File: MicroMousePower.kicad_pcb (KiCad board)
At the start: 2 copper layers, 59.6 x 56 mm, 103 parts, among them J1 USB_C_Receptacle_PowerOnly_6P, J2 Conn_02x16_Odd_Even, J3 Conn_01x02_Pin, Q1 TIP41C, Q2 TIP41C, Q3 TIP41C, U1 INA219AxDCN, U2 MCP73831-3-MC, U3 CH224K, U4 DRV8833PWPR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

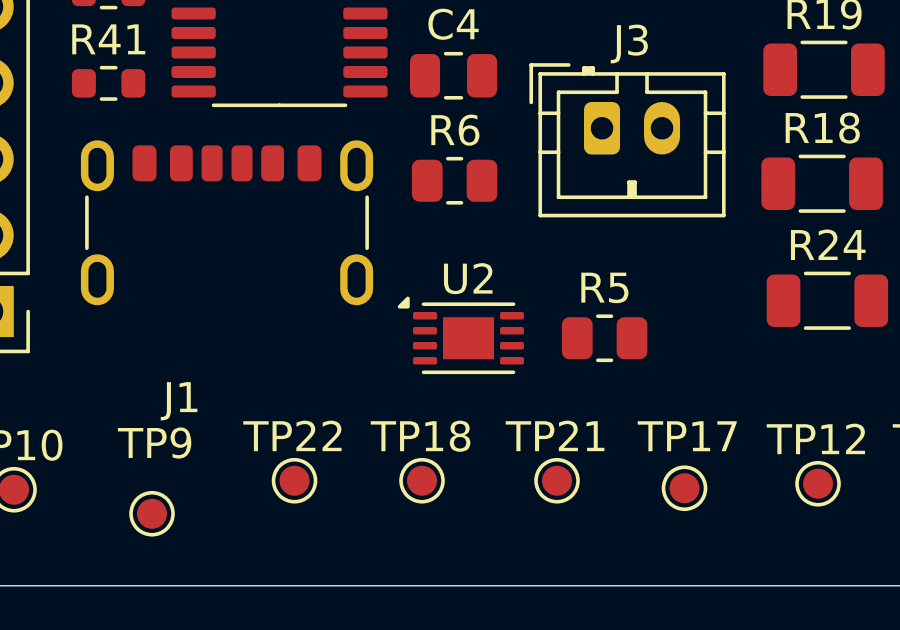
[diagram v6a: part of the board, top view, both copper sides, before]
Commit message: fixed another disconnect
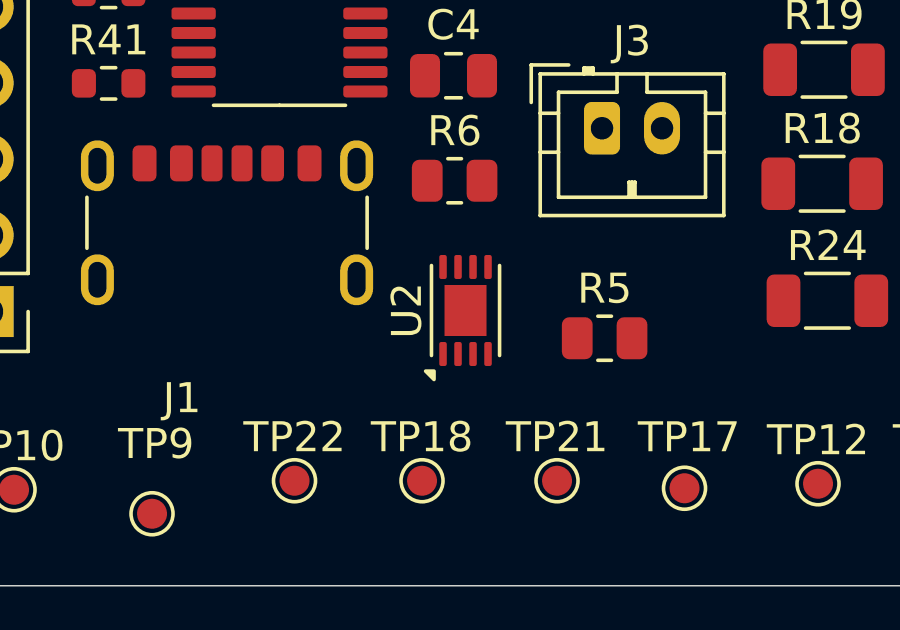
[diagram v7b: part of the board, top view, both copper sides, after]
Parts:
- moved U2 0.93 mm to (168.4, 108.8), turned to 90 degrees
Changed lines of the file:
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@@
 	(footprint "Package_DFN_QFN:DFN-8-1EP_3x2mm_P0.5mm_EP1.7x1.4mm"
 		(layer "F.Cu")
-		(at 168.55 109.75)
+		(at 168.45 108.825 90)
 		(descr "DFN, 8 Pin (http://ww1.microchip.com/downloads/en/DeviceDoc/8L_DFN_2x3x0_9_MC_C04-123C.pdf), generated with kicad-footprint-generator ipc_noLead_generator.py")
 		(tags "DFN NoLead")
 		(property "Reference" "U2"
-			(at 0 -1.95 0)
+			(at 0 -1.95 90)
 			(layer "F.SilkS")
 			(effects
@@
 		)
 		(property "Value" "MCP73831-3-MC"
-			(at 0 1.95 0)
+			(at 0 1.95 90)
 			(layer "F.Fab")
 			(effects
@@
 		)
 		(property "Datasheet" "http://ww1.microchip.com/downloads/en/DeviceDoc/20001984g.pdf"
-			(at 0 0 0)
+			(at 0 0 90)
 			(layer "F.Fab")
 			(hide yes)
@@
 		)
 		(property "Description" "Single cell, Li-Ion/Li-Po charge management controller, 4.35V, Tri-State Status Output, in DFN-8 package"
-			(at 0 0 0)
+			(at 0 0 90)
 			(layer "F.Fab")
 			(hide yes)
@@
 		)
 		(property "LCSC" "C635038"
-			(at 0 0 0)
+			(at 0 0 90)
 			(unlocked yes)
 			(layer "F.Fab")
@@
 		)
 		(fp_line
+			(start 2.1 -1.25)
+			(end -2.1 -1.25)
+			(stroke
+				(width 0.05)
+				(type solid)
+			)
+			(layer "F.CrtYd")
+		)
+		(fp_line
 			(start -2.1 -1.25)
 			(end -2.1 1.25)
@@
 		)
 		(fp_line
+			(start 2.1 1.25)
+			(end 2.1 -1.25)
+			(stroke
+				(width 0.05)
+				(type solid)
+			)
+			(layer "F.CrtYd")
+		)
+		(fp_line
 			(start -2.1 1.25)
 			(end 2.1 1.25)
@@
 		)
 		(fp_line
-			(start 2.1 -1.25)
-			(end -2.1 -1.25)
-			(stroke
-				(width 0.05)
-				(type solid)
-			)
-			(layer "F.CrtYd")
-		)
-		(fp_line
-			(start 2.1 1.25)
-			(end 2.1 -1.25)
-			(stroke
-				(width 0.05)
-				(type solid)
-			)
-			(layer "F.CrtYd")
+			(start 1.5 -1)
+			(end 1.5 1)
+			(stroke
+				(width 0.1)
+				(type solid)
+			)
+			(layer "F.Fab")
+		)
+		(fp_line
+			(start -1 -1)
+			(end 1.5 -1)
+			(stroke
+				(width 0.1)
+				(type solid)
+			)
+			(layer "F.Fab")
 		)
 		(fp_line
@@
 		)
 		(fp_line
+			(start 1.5 1)
+			(end -1.5 1)
+			(stroke
+				(width 0.1)
+				(type solid)
+			)
+			(layer "F.Fab")
+		)
+		(fp_line
 			(start -1.5 1)
 			(end -1.5 -0.5)
@@
 			(layer "F.Fab")
 		)
-		(fp_line
-			(start -1 -1)
-			(end 1.5 -1)
-			(stroke
-				(width 0.1)
-				(type solid)
-			)
-			(layer "F.Fab")
-		)
-		(fp_line
-			(start 1.5 -1)
-			(end 1.5 1)
-			(stroke
-				(width 0.1)
-				(type solid)
-			)
-			(layer "F.Fab")
-		)
-		(fp_line
-			(start 1.5 1)
-			(end -1.5 1)
-			(stroke
-				(width 0.1)
-				(type solid)
-			)
-			(layer "F.Fab")
-		)
 		(fp_text user "${REFERENCE}"
-			(at 0 0 0)
+			(at 0 0 90)
 			(layer "F.Fab")
 			(effects
@@
 		)
 		(pad "" smd roundrect
-			(at -0.425 -0.35)
-			(size 0.69 0.56)
-			(layers "F.Paste")
-			(roundrect_rratio 0.25)
-		)
-		(pad "" smd roundrect
-			(at -0.425 0.35)
-			(size 0.69 0.56)
-			(layers "F.Paste")
-			(roundrect_rratio 0.25)
-		)
-		(pad "" smd roundrect
-			(at 0.425 -0.35)
-			(size 0.69 0.56)
-			(layers "F.Paste")
-			(roundrect_rratio 0.25)
-		)
-		(pad "" smd roundrect
-			(at 0.425 0.35)
+			(at -0.425 -0.35 90)
+			(size 0.69 0.56)
+			(layers "F.Paste")
+			(roundrect_rratio 0.25)
+		)
+		(pad "" smd roundrect
+			(at -0.425 0.35 90)
+			(size 0.69 0.56)
+			(layers "F.Paste")
+			(roundrect_rratio 0.25)
+		)
+		(pad "" smd roundrect
+			(at 0.425 -0.35 90)
+			(size 0.69 0.56)
+			(layers "F.Paste")
+			(roundrect_rratio 0.25)
+		)
+		(pad "" smd roundrect
+			(at 0.425 0.35 90)
 			(size 0.69 0.56)
 			(layers "F.Paste")
@@
 		)
 		(pad "1" smd roundrect
-			(at -1.45 -0.75)
+			(at -1.45 -0.75 90)
 			(size 0.8 0.25)
 			(layers "F.Cu" "F.Mask" "F.Paste")
@@
 		)
 		(pad "2" smd roundrect
-			(at -1.45 -0.25)
+			(at -1.45 -0.25 90)
 			(size 0.8 0.25)
 			(layers "F.Cu" "F.Mask" "F.Paste")
@@
 		)
 		(pad "3" smd roundrect
-			(at -1.45 0.25)
+			(at -1.45 0.25 90)
 			(size 0.8 0.25)
 			(layers "F.Cu" "F.Mask" "F.Paste")
@@
 		)
 		(pad "4" smd roundrect
-			(at -1.45 0.75)
+			(at -1.45 0.75 90)
 			(size 0.8 0.25)
 			(layers "F.Cu" "F.Mask" "F.Paste")
@@
 		)
 		(pad "5" smd roundrect
-			(at 1.45 0.75)
+			(at 1.45 0.75 90)
 			(size 0.8 0.25)
 			(layers "F.Cu" "F.Mask" "F.Paste")
@@
 		)
 		(pad "6" smd roundrect
-			(at 1.45 0.25)
+			(at 1.45 0.25 90)
 			(size 0.8 0.25)
 			(layers "F.Cu" "F.Mask" "F.Paste")
@@
 		)
 		(pad "7" smd roundrect
-			(at 1.45 -0.25)
+			(at 1.45 -0.25 90)
 			(size 0.8 0.25)
 			(layers "F.Cu" "F.Mask" "F.Paste")
@@
 		)
 		(pad "8" smd roundrect
-			(at 1.45 -0.75)
+			(at 1.45 -0.75 90)
 			(size 0.8 0.25)
 			(layers "F.Cu" "F.Mask" "F.Paste")
@@
 		)
 		(pad "9" smd rect
-			(at 0 0)
+			(at 0 0 90)
 			(size 1.7 1.4)
 			(property pad_prop_heatsink)

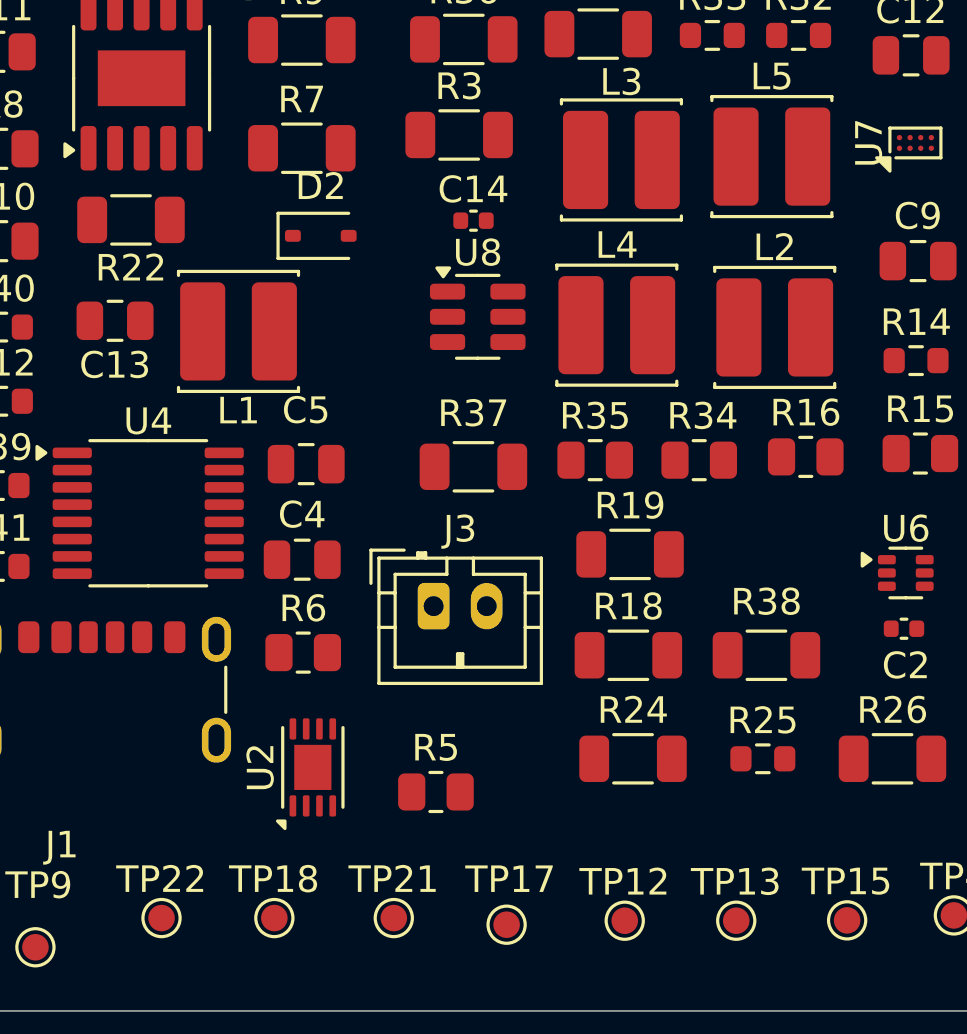
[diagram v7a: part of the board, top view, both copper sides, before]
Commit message: updated schematic due to ordering error
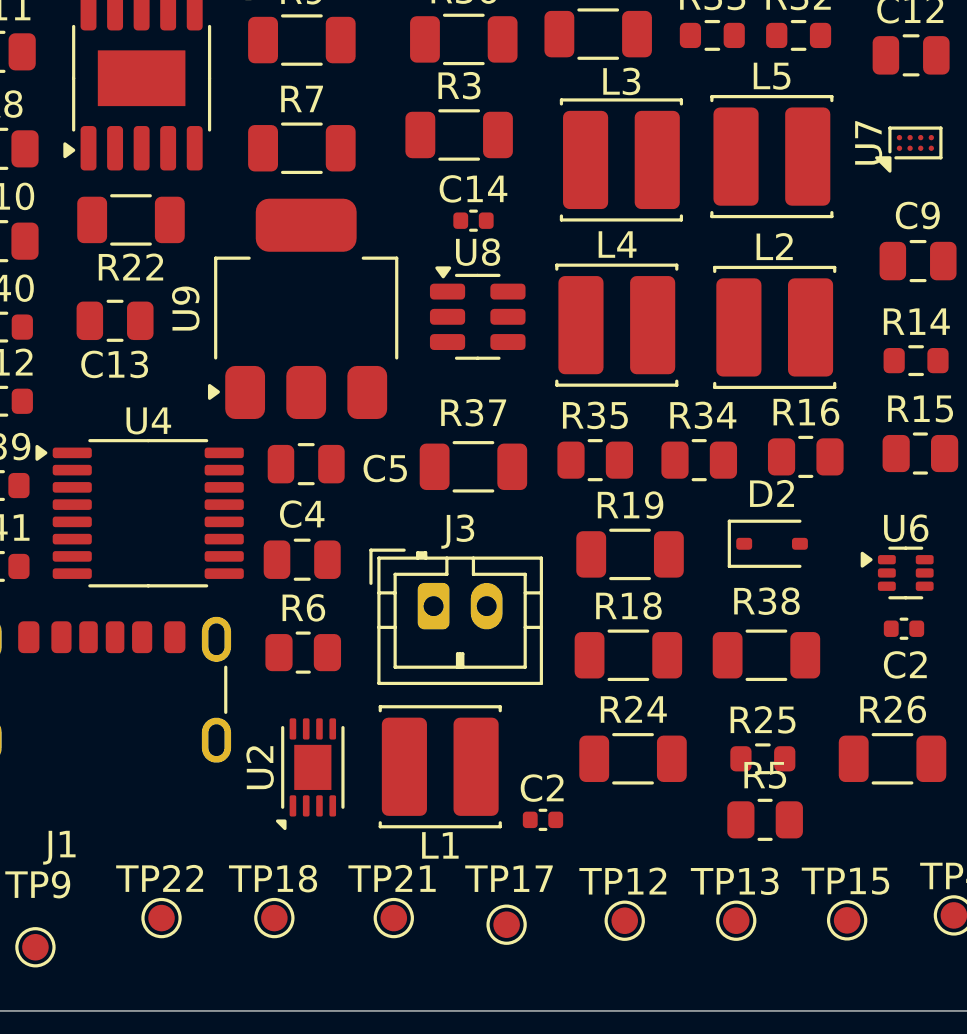
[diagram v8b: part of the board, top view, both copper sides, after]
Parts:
- added C2: 1u, Capacitor_SMD:C_0402_1005Metric, F.Cu at (177.1, 110.8)
- added U9: TC1262-33, Package_TO_SOT_SMD:SOT-223-3_TabPin2, F.Cu at (168.2, 91.5)
- moved D2 20.6 mm to (185.8, 100.4)
- moved L1 18.1 mm to (173.2, 108.8)
- moved R5 12.4 mm to (185.5, 110.8)
